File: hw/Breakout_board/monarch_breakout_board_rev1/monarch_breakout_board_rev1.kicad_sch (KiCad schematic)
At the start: 11 parts, among them J108 Conn_01x03

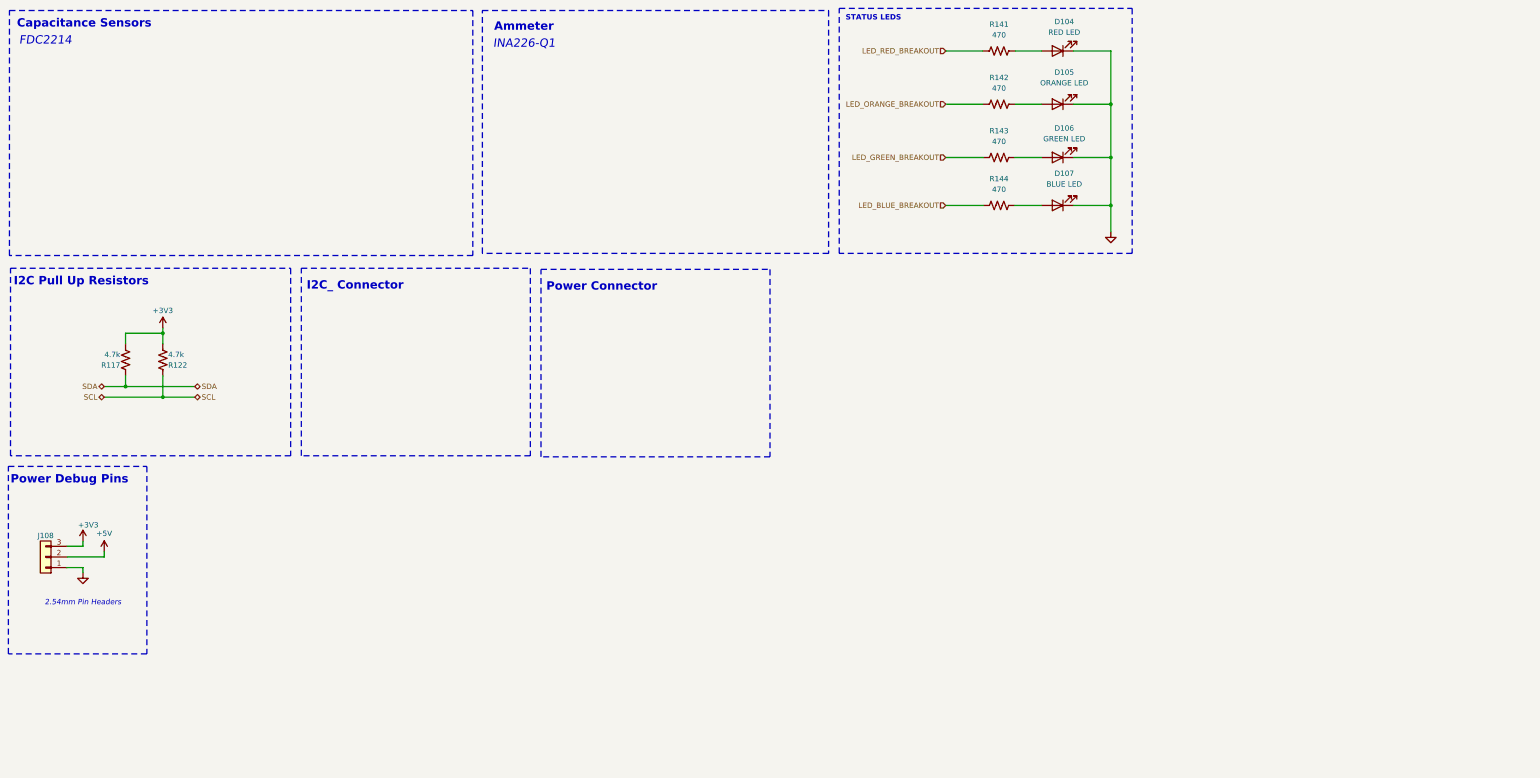
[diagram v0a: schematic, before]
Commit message: Added FDC2214 + INA-226-Q1 to schematic
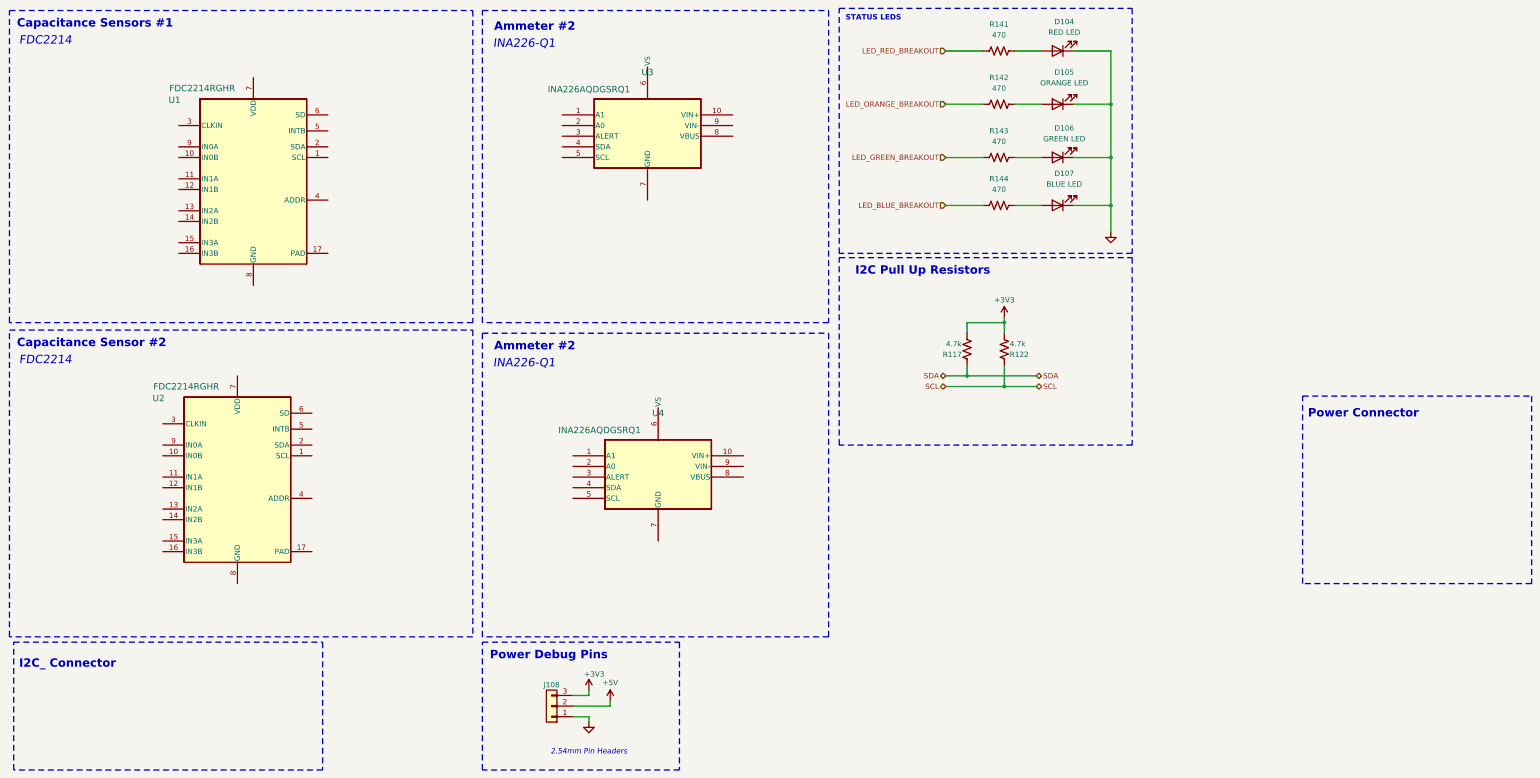
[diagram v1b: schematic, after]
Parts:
- added U1, U2: FDC2214RGHR, RGH0016A, symbol FDC2214:FDC2214RGHR
- added U3, U4: INA226AQDGSRQ1, DGS10_TEX, symbol INA226-Q1:INA226AQDGSRQ1
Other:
- note added: "Ammeter #2"
- note added: "Capacitance Sensor #2"
- note added: "Capacitance Sensors #1"
- note removed: "Ammeter"
- note removed: "Capacitance Sensors"
- moved on the sheet: J108, R117, R122

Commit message: Breakout Board Work
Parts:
- removed D105: ORANGE LED, LED_SMD:LED_0603_1608Metric, symbol Device:LED
- removed D106: GREEN LED, LED_SMD:LED_0603_1608Metric, symbol Device:LED
- removed D107: BLUE LED, LED_SMD:LED_0603_1608Metric, symbol Device:LED
- removed R142, R143, R144: 470, Resistor_SMD:R_0603_1608Metric, symbol Device:R_US
- added C1: 1uF, symbol Device:C
- added C2: C, symbol Device:C
- added C3, C4: 0.01 uF, symbol Device:C
- added J14: 5037630491, CONN_5037630000-SD_04_MOL, symbol 5037630491:5037630491
- added L1: L, symbol Device:L
- added R1: R_US, symbol Device:R_US
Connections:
- net LED_RED_BREAKOUT is gone; now on net +3V3: R141.1
- net SCL is gone; now on net I2C4_SCL: R122.2
- net SDA is gone; now on net I2C4_SDA: R117.2
- net +3V3: now also J14.4
- net GND: now also U2.8 (GND), U4.7 (GND), C1.1, C3.1, C4.1, J14.3
- net I2C4_SDA: now reaches U4.4 (SDA)
- net I2C4_SDA: now also U2.2 (SDA), J14.1
- net I2C4_SCL: now reaches U4.5 (SCL)
- net I2C4_SCL: now also U2.1 (SCL), J14.2
- net +3.3V: now reaches U4.6 (VS)
- net +3.3V: now also U2.7 (VDD), C1.2, C3.2, C4.2
- net +5V: no longer names the net of J108.2 (Pin_2)
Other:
- note added: "PIB Connection"
- note added: "POWER LED"
- note added: "What does this alert do"
- note added: "What is the 10A load on the data sheet??"
- note added: "What resistor should we use this is based on the current we'll be expecting to read..."
- note added: "do we want a clock?"
- note added: "out of curiosity what is this LC circuit for?"
- note removed: "I2C_ Connector"
- note removed: "Power Connector"
- note removed: "STATUS LEDS"
- moved on the sheet: D104, J108, R117, R122, R141, U2, U3, U4

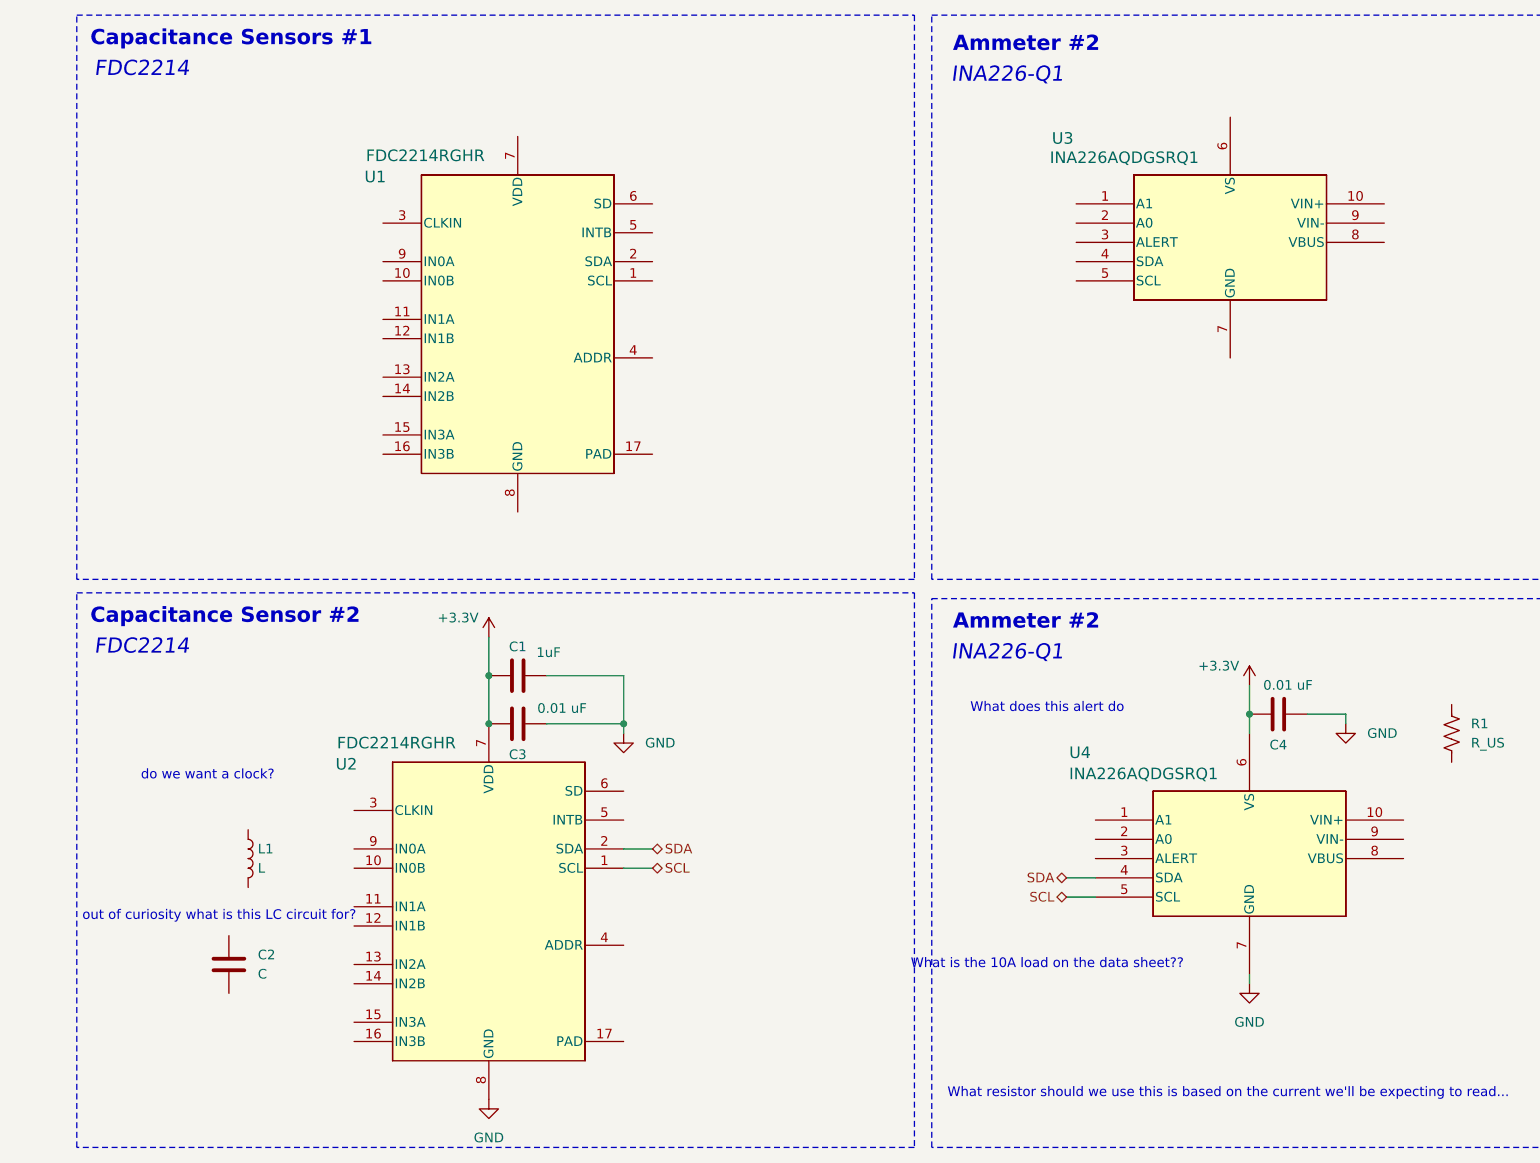
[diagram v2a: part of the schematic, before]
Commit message: FDC2214 LC Tank Work
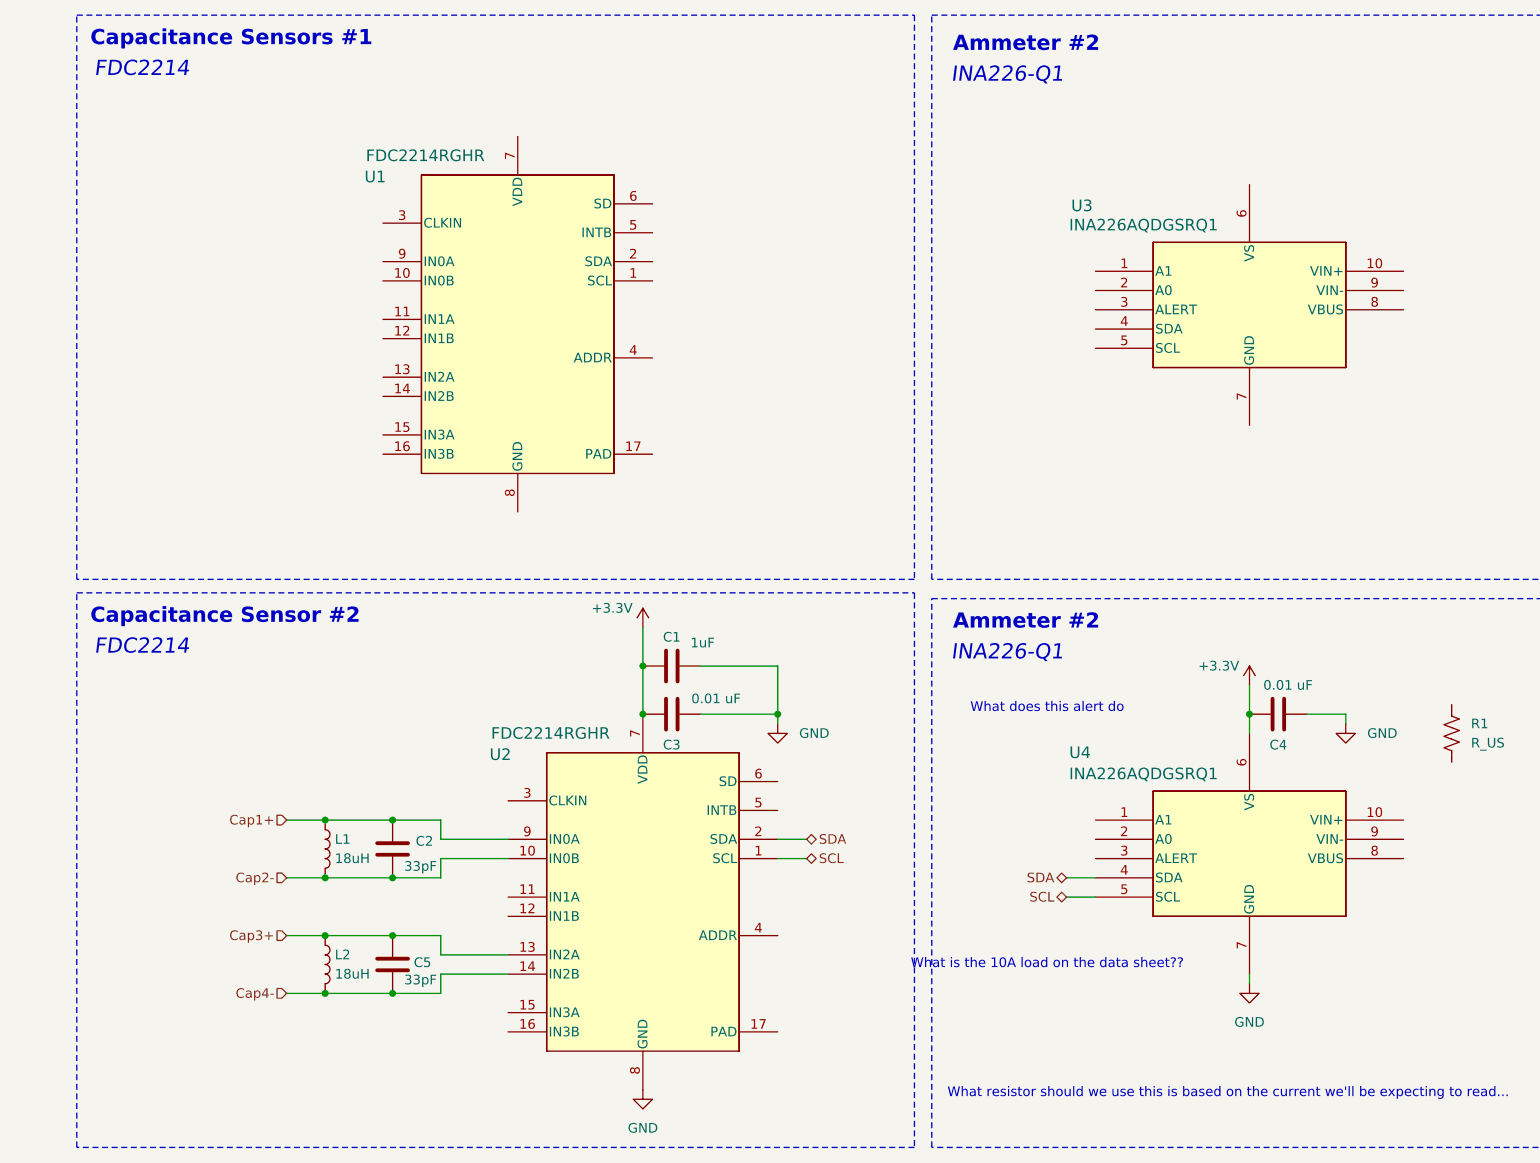
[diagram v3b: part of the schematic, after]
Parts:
- added C5: 33pF, symbol Device:C
- added L2: 18uH, symbol Device:L
- C2: value C -> 33pF
- L1: value L -> 18uH
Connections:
- net Cap1+: now reaches L1.1
- net Cap1+: now also C2.1, U2.9 (IN0A)
- net Cap2-: now reaches L1.2
- net Cap2-: now also C2.2, U2.10 (IN0B)
- net Cap3+: now reaches U2.13 (IN2A)
- net Cap3+: now also C5.1, L2.1
- net Cap4-: now reaches U2.14 (IN2B)
- net Cap4-: now also C5.2, L2.2
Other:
- note removed: "do we want a clock?"
- note removed: "out of curiosity what is this LC circuit for?"
- moved on the sheet: C1, C2, C3, L1, U2, U3

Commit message: Schematic Work + Cleanup + Initial PCB Design
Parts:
- removed R1: R_US, symbol Device:R_US
- removed U1: FDC2214RGHR, RGH0016A, symbol FDC2214:FDC2214RGHR
- added C10, C9: 33pF, Capacitor_SMD:C_0603_1608Metric, symbol Device:C
- added C8: 0.01 uF, Capacitor_SMD:C_0603_1608Metric, symbol Device:C
- added L5, L6: 18uH, symbol Device:L
- added R2, R3: ?, Resistor_SMD:R_0402_1005Metric, symbol Device:R_US
- C1, C2, C3, C4, C5: footprint (none) -> Capacitor_SMD:C_0603_1608Metric
- J14: footprint CONN_5037630000-SD_04_MOL -> Connector 4 Pin:CONN_5037630000-SD_04_MOL
- R117, R122, R141: footprint Resistor_SMD:R_0603_1608Metric -> Resistor_SMD:R_0402_1005Metric
- U2: footprint RGH0016A -> FDC2214:RGH0016A
- U3, U4: footprint DGS10_TEX -> INA226-Q1:DGS10_TEX
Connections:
- net +3.3V: now also U3.6 (VS), U4.2 (A0), C8.2
- net Cap1+: now also C9.1, L5.1; no longer C2.1, L1.1
- net Cap2-: now also C9.2, L5.2; no longer C2.2, L1.2
- net Cap3+: now also U2.11 (IN1A), C10.1, L6.1; no longer C5.1, L2.1, U2.13 (IN2A)
- net Cap4-: now also U2.12 (IN1B), C10.2, L6.2; no longer C5.2, L2.2, U2.14 (IN2B)
- net GND: now also U2.17 (PAD), U3.1 (A1), U3.2 (A0), U3.7 (GND), U3.9 (VIN-), U4.1 (A1), U4.9 (VIN-), C8.1, R2.2, R3.2
- net I2C4_SCL: now also U3.5 (SCL)
- net I2C4_SDA: now also U3.4 (SDA)
- net Electro2: now reaches U4.10 (VIN+)
- net Electro2: now also U4.8 (VBUS), R3.1
- net Electro1: now reaches U3.10 (VIN+)
- net Electro1: now also U3.8 (VBUS), R2.1
- net Cap7+: now reaches U2.15 (IN3A)
- net Cap7+: now also C5.1, L2.1
- net Cap8-: now reaches U2.16 (IN3B)
- net Cap8-: now also C5.2, L2.2
- new net Cap5+: C2.1, L1.1, U2.13 (IN2A)
- new net Cap6-: C2.2, L1.2, U2.14 (IN2B)
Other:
- note added: "Ammeter #1"
- note added: "Capacitance Sensor (Feed System)"
- note added: "I2C Addr: 0x2A"
- note added: "I2C Addr: 0x40"
- note added: "I2C Addr: 0x41"
- note removed: "Capacitance Sensor #2"
- note removed: "Capacitance Sensors #1"
- note removed: "What is the 10A load on the data sheet??"
- moved on the sheet: C1, C2, C3, C5, L1, L2, U2

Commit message: Footprints, Connectors, and Routing
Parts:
- removed J108: Conn_01x03, Connector_PinSocket_2.54mm:PinSocket_1x03_P2.54mm_Vertical, symbol Connector_Generic:Conn_01x03
- removed J14: 5037630491, Connector 4 Pin:CONN_5037630000-SD_04_MOL, symbol 5037630491:5037630491
- L1, L2, L5, L6: footprint (none) -> Inductor_SMD:L_0805_2012Metric
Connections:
- net GND: now also U2.4 (ADDR)
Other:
- added sheet Connectors (untitled.kicad_sch)
- note added: "Breakout Board Connectors"
- note added: "More then needed. If we need more connections"
- note added: "Need to look into the exact inductors needed, the footprint size, and the specs"
- note removed: "2.54mm Pin Headers"
- note removed: "PIB Connection"
- note removed: "Power Debug Pins"
- moved on the sheet: C4, C8, D104, R141, R3, U3, U4
